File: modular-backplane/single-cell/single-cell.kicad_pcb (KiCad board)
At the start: 2 copper layers, 12 x 12 mm, 6 parts, among them J1 To Backplane, U1 ATtiny404-SS

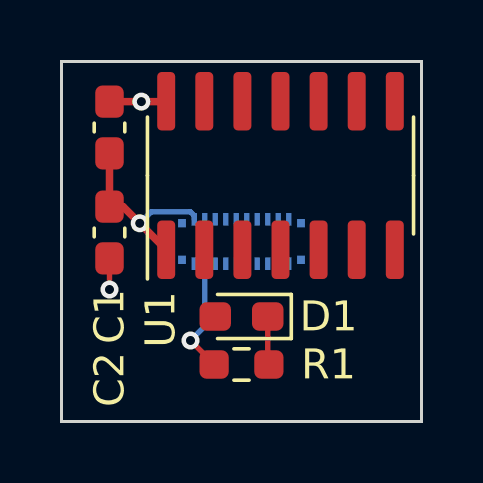
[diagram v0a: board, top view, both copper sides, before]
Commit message: (Re)route single-cell module; add grabbing holes and markings
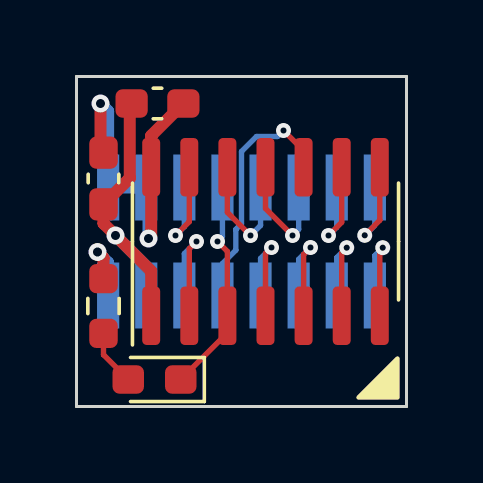
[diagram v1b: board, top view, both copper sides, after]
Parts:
- added H1: Pull, agausmann:Hole_Cell, F.Cu at (156.1, 91.5)
- added H2: Pull, agausmann:Hole_Cell, F.Cu at (156.0, 100.5)
- J1: footprint agausmann:Molex_SlimStack_216701-0209_02x10_P0.35mm_Vertical -> agausmann:XKB_X1321FVS_02x08_P1.27mm_Vertical
- moved R1 5.00 mm to (151.4, 98.2), turned to -90 degrees
- moved C2 4.59 mm to (153.2, 91.4), turned to 0 degrees
- moved D1 3.58 mm to (153.1, 100.6)
- moved U1 2.26 mm to (156.8, 96.0)
- moved C1 1.71 mm to (151.4, 93.9)
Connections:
- C1 pad 1: VCC -> +5V
- C2 pad 1: VCC -> +5V
- D1 pad 1: Net-(D1-Pad1) -> /STATE
- D1 pad 2: /STATE -> Net-(D1-Pad2)
- J1 pad 1: /X1 -> /IN7
- J1 pad 10: unconnected-(J1-Pad10) -> /STATE
- J1 pad 11: unconnected-(J1-Pad11) -> /CLK
- J1 pad 12: unconnected-(J1-Pad12) -> /INIT
- J1 pad 13: unconnected-(J1-Pad13) -> +5V
- J1 pad 14: /STATE -> GND
- J1 pad 15: /NRST -> /VLED
- J1 pad 16: /TOGGLE -> GND
- J1 pad 2: /X2 -> /IN6
- J1 pad 3: /X3 -> /IN0
- J1 pad 4: /X4 -> /IN5
- J1 pad 5: /X5 -> /IN1
- J1 pad 6: /X6 -> /IN4
- J1 pad 7: /X7 -> /IN2
- J1 pad 8: /X8 -> /IN3
- J1 pad 9: unconnected-(J1-Pad9) -> /NRST
- R1 pad 2: Net-(D1-Pad1) -> Net-(D1-Pad2)
- U1 pad 1: VCC -> +5V
- U1 pad 11: unconnected-(U1-Pad11) -> /IN4
- U1 pad 12: unconnected-(U1-Pad12) -> /IN3
- U1 pad 13: unconnected-(U1-Pad13) -> /INIT
- U1 pad 2: /TOGGLE -> /CLK
- U1 pad 4: unconnected-(U1-Pad4) -> /IN2
- U1 pad 5: unconnected-(U1-Pad5) -> /IN1
- U1 pad 6: unconnected-(U1-Pad6) -> /IN0
- U1 pad 7: unconnected-(U1-Pad7) -> /IN7
- U1 pad 8: unconnected-(U1-Pad8) -> /IN6
- U1 pad 9: unconnected-(U1-Pad9) -> /IN5
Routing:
- net +5V: track 0.00 -> 10.5 mm, vias 0 -> 1
- net GND: track 2.93 -> 12.6 mm
- net /NRST: track 0.00 -> 8.26 mm, vias 0 -> 1
- net /STATE: track 0.00 -> 7.25 mm, vias 0 -> 1
- net VCC: track 6.41 -> 0.00 mm, vias 1 -> 0
- net /CLK: track 0.00 -> 4.54 mm, vias 0 -> 1
- net /IN4: track 0.00 -> 4.33 mm, vias 0 -> 1
- net /IN3: track 0.00 -> 4.33 mm, vias 0 -> 1
- net /IN6: track 0.00 -> 4.21 mm, vias 0 -> 1
- net /INIT: track 0.00 -> 4.19 mm, vias 0 -> 1
- net /IN5: track 0.00 -> 4.17 mm, vias 0 -> 1
- net /IN1: track 0.00 -> 4.13 mm, vias 0 -> 1
- net /IN2: track 0.00 -> 4.11 mm, vias 0 -> 1
- net /IN0: track 0.00 -> 4.07 mm, vias 0 -> 1
- net /IN7: track 0.00 -> 4.01 mm, vias 0 -> 1
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- removed copper zone on B.Cu, net GND
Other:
- board size 12 x 12 mm -> 11 x 11 mm
- board text added: "0207"
- board text added: "2023"
- board text added: "AG"
- board text added: "HWL"
